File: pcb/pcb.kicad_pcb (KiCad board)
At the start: 2 copper layers, 159.6 x 112.3 mm, 31 parts, among them J1 Conn_01x10, J2 Conn_01x05, J3 Conn_01x05, J4 Conn_01x05, J5 Conn_01x05, J6 Conn_01x05, J7 Conn_01x05, J8 Conn_01x10, U1 teensy-2.0

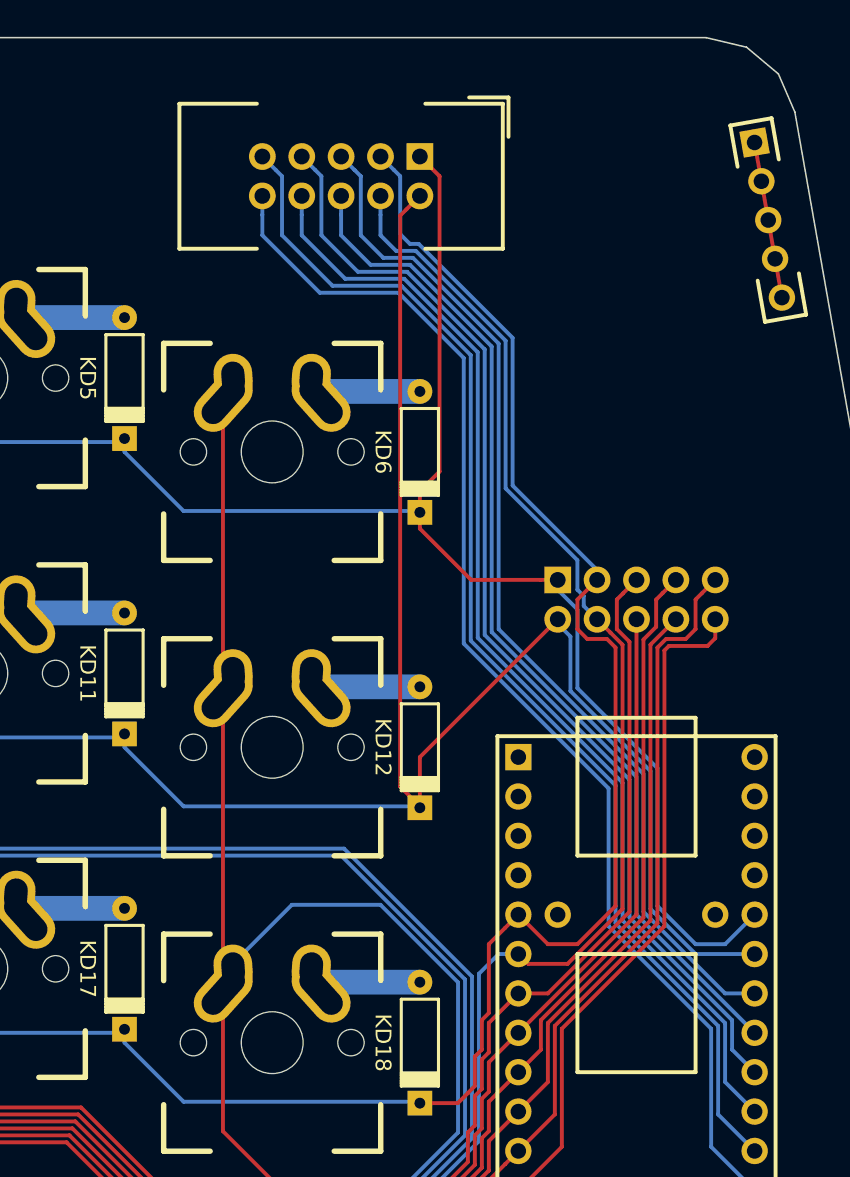
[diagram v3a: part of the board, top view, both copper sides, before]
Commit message: Rotate header to avoid twisting ribbon cable
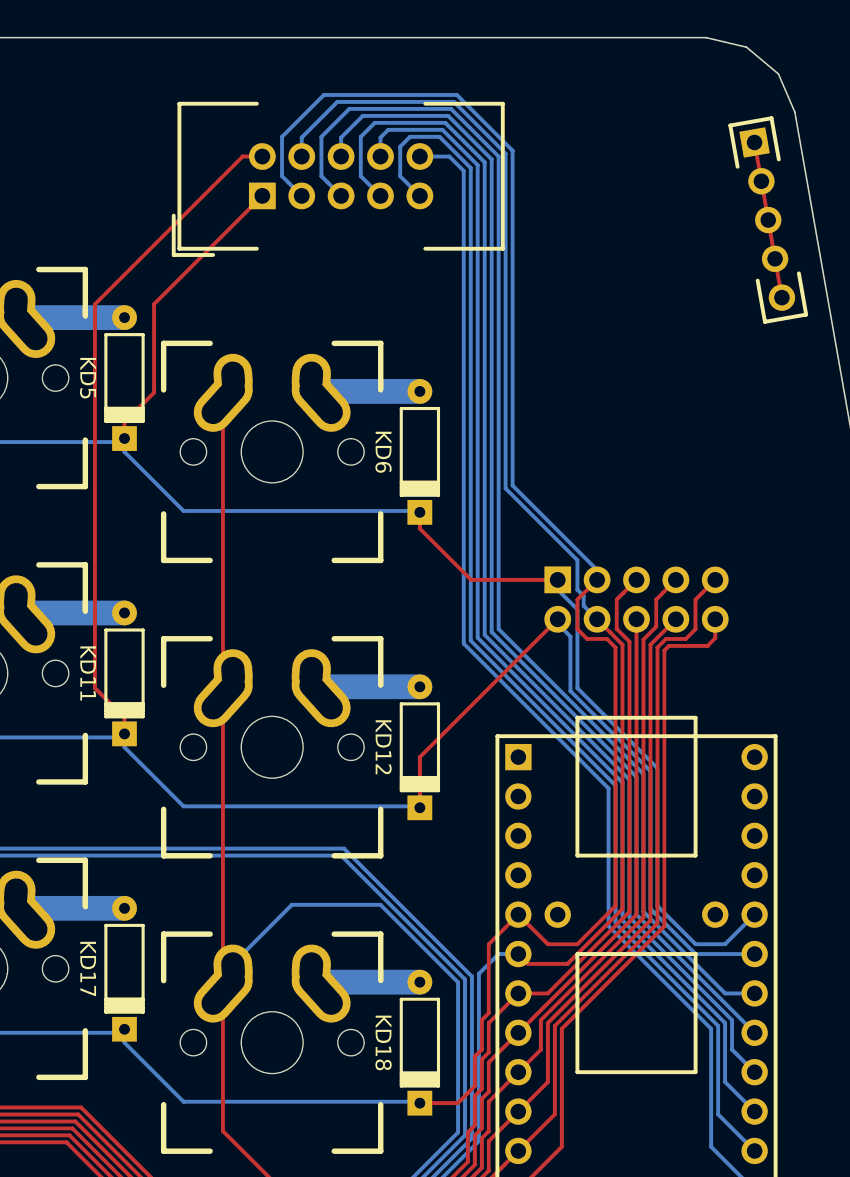
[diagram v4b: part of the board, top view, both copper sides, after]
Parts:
- moved J1 2.54 mm to (-5.08, -64.1), turned to 180 degrees
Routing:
- net /R2: track 194.3 -> 212.6 mm
- net /R3: track 329.3 -> 344.6 mm
- net Net-(J1-Pad5): track 67.3 -> 79.7 mm
- net Net-(J1-Pad6): track 66.5 -> 76.0 mm
- net Net-(J1-Pad7): track 73.0 -> 79.6 mm
- net /R0: track 180.8 -> 176.1 mm
- net Net-(J1-Pad8): track 73.4 -> 77.1 mm
- net Net-(J1-Pad10): track 80.3 -> 76.7 mm
- net /R1: track 198.6 -> 201.4 mm

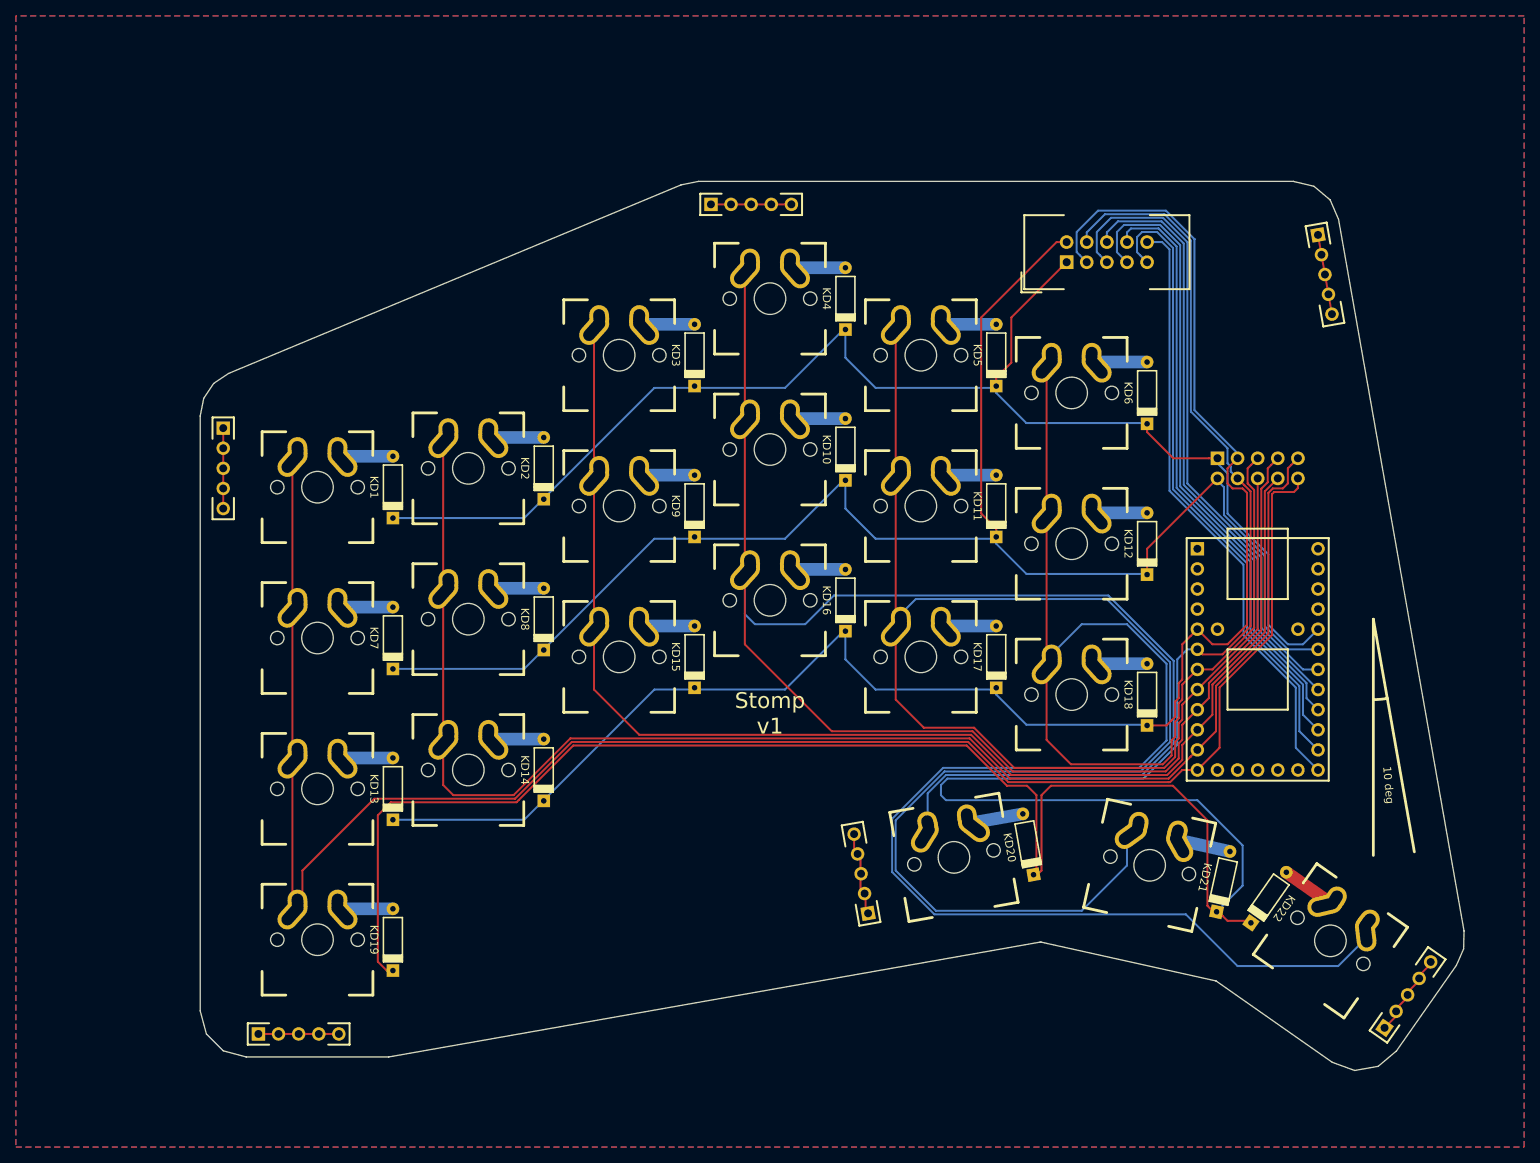
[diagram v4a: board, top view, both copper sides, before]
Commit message: Update board outline
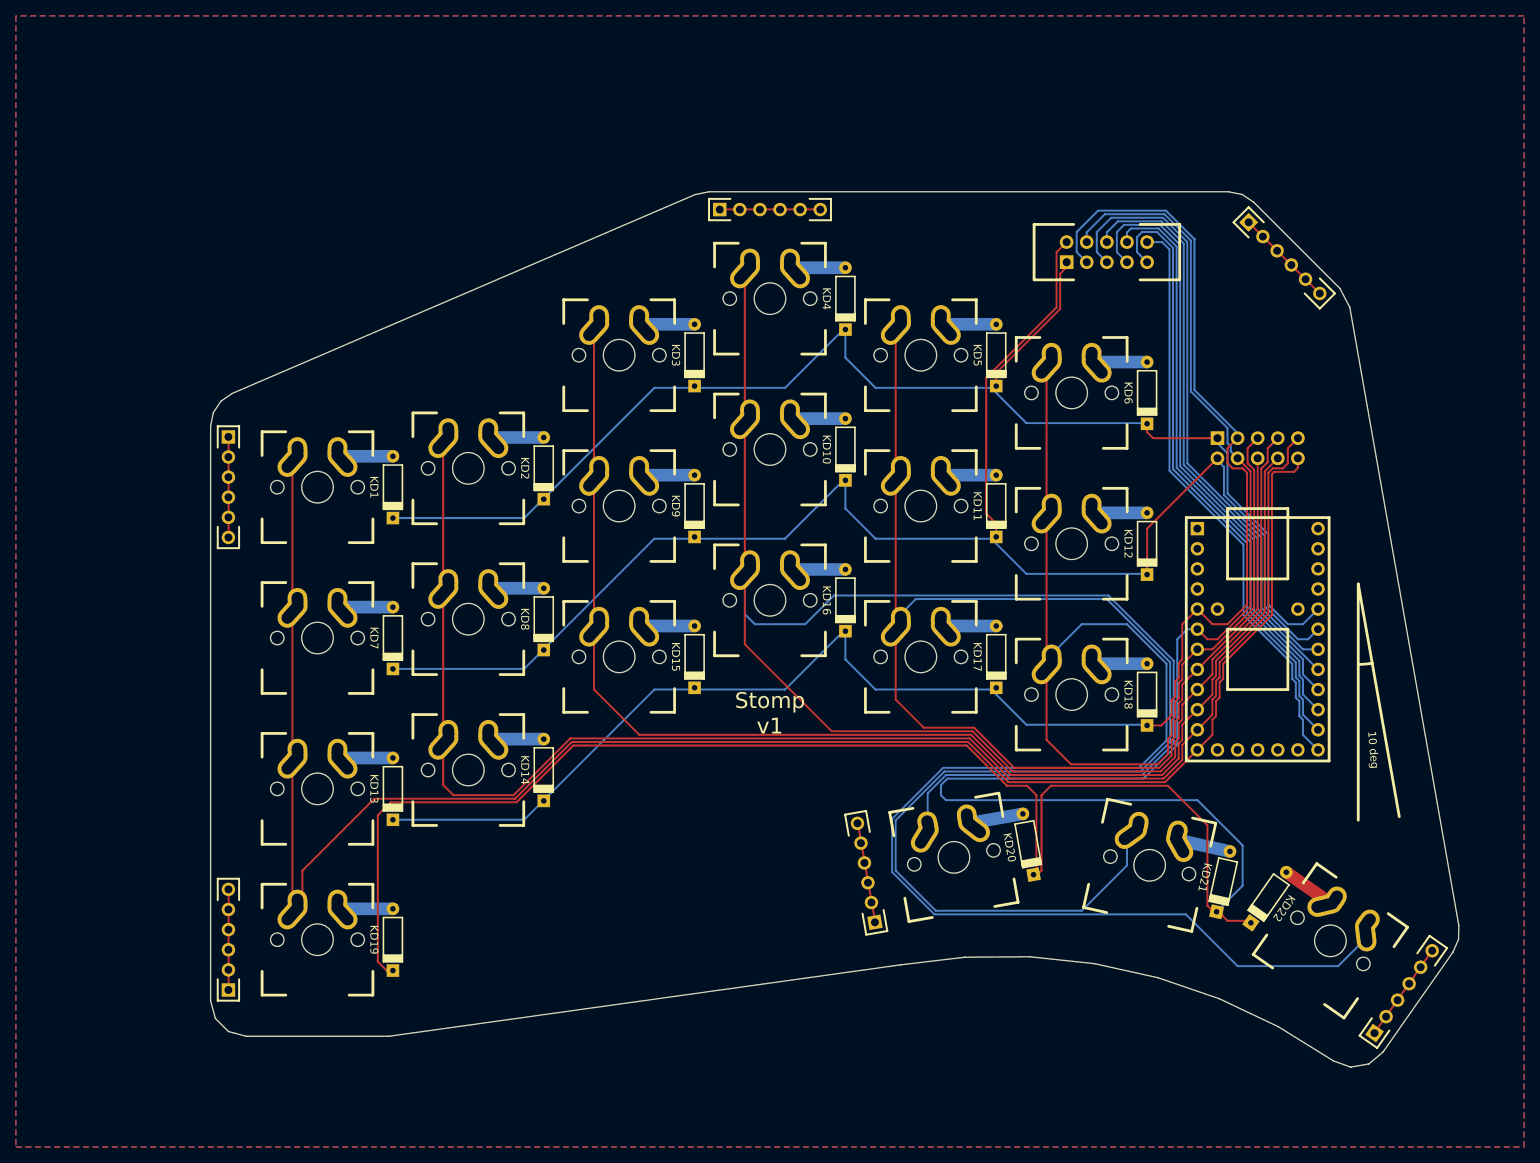
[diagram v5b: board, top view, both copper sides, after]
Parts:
- J2, J3, J4, J5, J6, J7: value Conn_01x05 -> Conn_01x06; footprint keyboard-parts:header_1x05_2.54mm -> keyboard-parts:header_1x06_2.54mm
- moved J7 8.90 mm to (12.8, -69.2), turned to 45 degrees
- moved J4 6.73 mm to (-116.0, 27.8), turned to 180 degrees
- moved U1 2.54 mm to (14.0, -16.5)
- moved J5 1.43 mm to (-34.4, 19.2)
- moved J6 1.43 mm to (28.7, 33.2)
- moved J2 1.29 mm to (-54.0, -70.8)
- moved J3 1.29 mm to (-116.0, -42.1)
- moved J8 1.27 mm to (14.0, -40.6)
- moved J1 1.27 mm to (-5.08, -65.4)
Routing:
- net Net-(J4-Pad1): track 9.84 -> 12.7 mm
- net Net-(J2-Pad1): track 9.84 -> 12.7 mm
- net Net-(J3-Pad1): track 9.84 -> 12.7 mm
- net Net-(J7-Pad1): track 10.2 -> 12.8 mm
- net Net-(J1-Pad9): track 80.3 -> 77.8 mm
- net Net-(J1-Pad5): track 79.7 -> 77.2 mm
- net Net-(J1-Pad6): track 76.0 -> 73.5 mm
- net Net-(J1-Pad8): track 77.1 -> 74.5 mm
- net Net-(J1-Pad10): track 76.7 -> 74.2 mm
- net Net-(J1-Pad7): track 79.6 -> 77.1 mm
- net Net-(J5-Pad1): track 10.3 -> 12.6 mm
- net /C2-C9: track 164.3 -> 166.5 mm
- net /C1-CA: track 187.2 -> 189.4 mm
- net /C5-C6: track 247.9 -> 250.1 mm
- net /C3-C8: track 264.0 -> 266.2 mm
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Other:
- board size 159.6 x 112.3 mm -> 157.6 x 110.6 mm

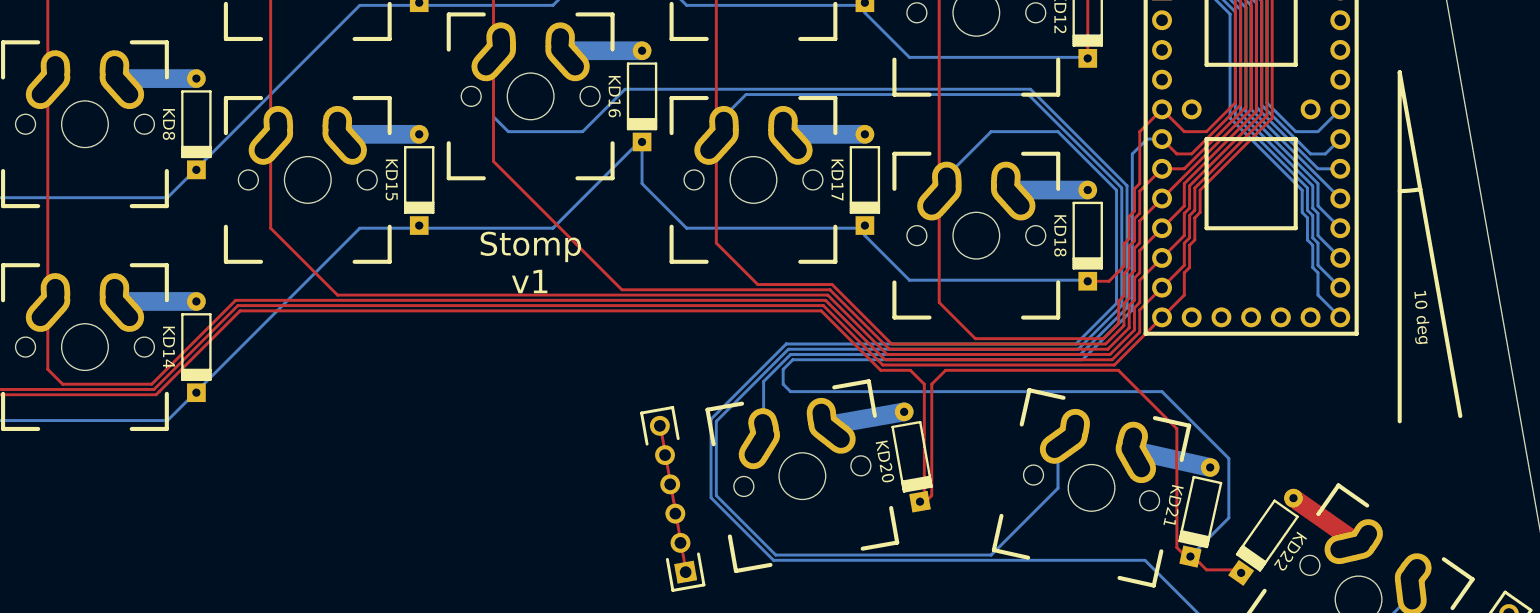
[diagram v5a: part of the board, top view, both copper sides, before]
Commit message: Add logos to main pcb
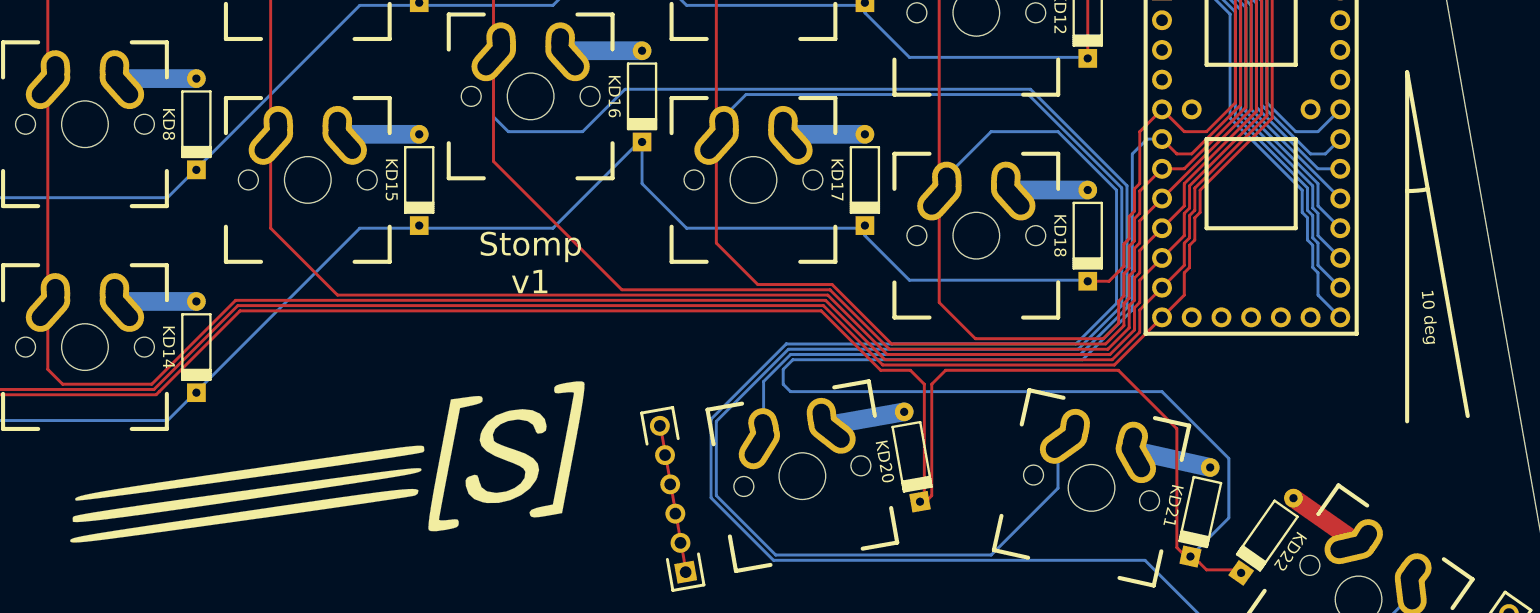
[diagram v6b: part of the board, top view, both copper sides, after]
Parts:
- added G***: LOGO, logos:smark-rev, F.Cu at (-64.8, 11.4)
- added G***: LOGO, logos:smark, B.Cu at (-64.8, 11.4)
